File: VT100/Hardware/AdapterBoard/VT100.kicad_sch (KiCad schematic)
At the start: 40 parts, among them J1 GPIO, J2 RS232, J3 Vin < 12V DC / AC, J4 Mini-DIN-6, J5 zu Pi Zero, J6 USB_A, J7 Z80-MBC2 direct, J8 LCD Power, J9 On / Off, K1 G5V-2, Q2 BC546, Q3 BS170, U1 LM2576HVS-ADJ

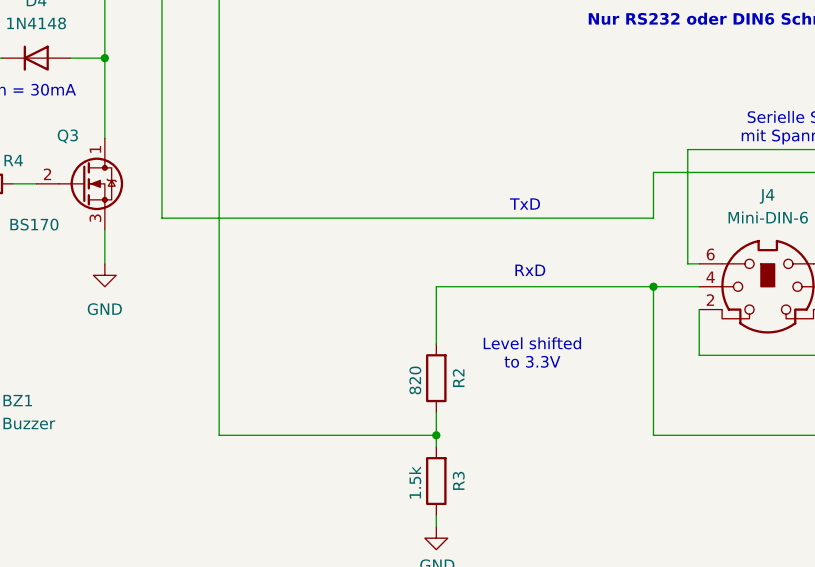
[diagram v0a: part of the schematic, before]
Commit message: VT100 AdapterBoard: add TxD level shifter
Add TxD level shifting network in AdapterBoard schematic and PCB routing.\n\nChanges include new resistor-based shift path and corresponding net/routing updates for TXD signal adaptation.
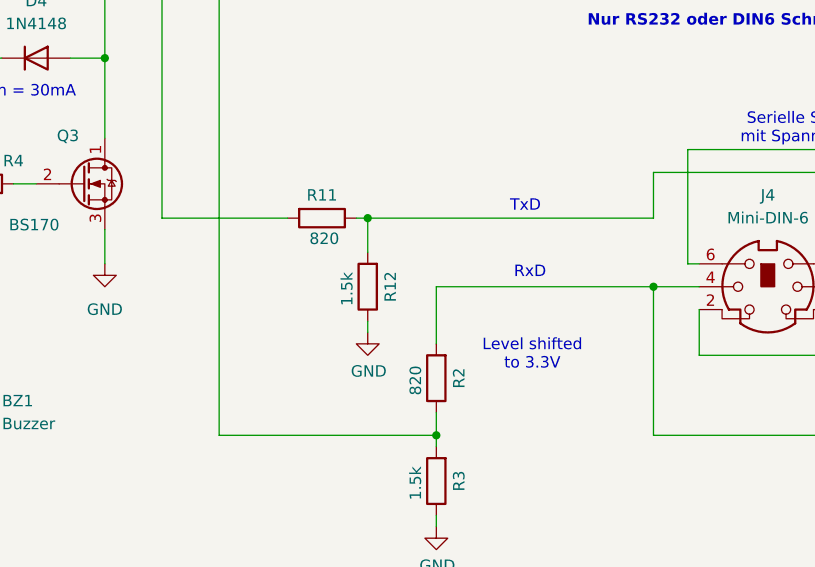
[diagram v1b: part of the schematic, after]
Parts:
- added R11: 820, Resistor_THT:R_Axial_DIN0207_L6.3mm_D2.5mm_P10.16mm_Horizontal, symbol Device:R
- added R12: 1.5k, Resistor_THT:R_Axial_DIN0207_L6.3mm_D2.5mm_P10.16mm_Horizontal, symbol Device:R
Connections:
- net GND: now also R12.1
- net at J2.2 (Pin_2), K1.6, K1.9: now also R11.2; no longer J4.3, J7.3 (Pin_3)
- new net: J4.3, J7.3 (Pin_3), R11.1, R12.2
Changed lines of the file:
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@@
 	)
 	(junction
+		(at 171.45 74.93)
+		(diameter 0)
+		(color 0 0 0 0)
+	)
+	(junction
 		(at 142.24 57.15)
 		(diameter 0)
@@
 	(wire
 		(pts
+			(xy 170.18 74.93) (xy 171.45 74.93)
+		)
+		(stroke
+			(width 0)
+			(type default)
+		)
+	)
+	(wire
+		(pts
 			(xy 73.66 35.56) (xy 82.55 35.56)
 		)
@@
 	(wire
 		(pts
+			(xy 171.45 74.93) (xy 171.45 78.74)
+		)
+		(stroke
+			(width 0)
+			(type default)
+		)
+	)
+	(wire
+		(pts
 			(xy 179.07 96.52) (xy 179.07 99.06)
 		)
@@
 	(wire
 		(pts
+			(xy 171.45 86.36) (xy 171.45 87.63)
+		)
+		(stroke
+			(width 0)
+			(type default)
+		)
+	)
+	(wire
+		(pts
 			(xy 58.42 38.1) (xy 60.96 38.1)
 		)
@@
 	(wire
 		(pts
+			(xy 171.45 74.93) (xy 203.2 74.93)
+		)
+		(stroke
+			(width 0)
+			(type default)
+		)
+	)
+	(wire
+		(pts
 			(xy 208.28 90.17) (xy 224.79 90.17)
 		)
@@
 	(wire
 		(pts
-			(xy 148.59 74.93) (xy 203.2 74.93)
+			(xy 148.59 74.93) (xy 162.56 74.93)
 		)
 		(stroke
@@
 	)
 	(symbol
+		(lib_id "Device:R")
+		(at 166.37 74.93 270)
+		(unit 1)
+		(exclude_from_sim no)
+		(in_bom yes)
+		(on_board yes)
+		(dnp no)
+		(property "Reference" "R11"
+			(at 166.37 72.39 90)
+			(effects
+				(font
+					(size 1.27 1.27)
+				)
+			)
+		)
+		(property "Value" "820"
+			(at 166.624 77.216 90)
+			(effects
+				(font
+					(size 1.27 1.27)
+				)
+			)
+		)
+		(property "Footprint" "Resistor_THT:R_Axial_DIN0207_L6.3mm_D2.5mm_P10.16mm_Horizontal"
+			(at 166.37 73.152 90)
+			(effects
+				(font
+					(size 1.27 1.27)
+				)
+				(hide yes)
+			)
+		)
+		(property "Datasheet" "~"
+			(at 166.37 74.93 0)
+			(effects
+				(font
+					(size 1.27 1.27)
+				)
+				(hide yes)
+			)
+		)
+		(property "Description" "Resistor"
+			(at 166.37 74.93 0)
+			(effects
+				(font
+					(size 1.27 1.27)
+				)
+				(hide yes)
+			)
+		)
+		(pin "2"
+		)
+		(pin "1"
+		)
+		(instances
+			(project "VT100"
+				(path "/e63e39d7-6ac0-4ffd-8aa3-1841a4541b55"
+					(reference "R11")
+					(unit 1)
+				)
+			)
+		)
+	)
+	(symbol
 		(lib_id "Mechanical:MountingHole")
 		(at 245.11 151.13 0)
@@
 	(symbol
 		(lib_id "Device:R")
+		(at 171.45 82.55 180)
+		(unit 1)
+		(exclude_from_sim no)
+		(in_bom yes)
+		(on_board yes)
+		(dnp no)
+		(property "Reference" "R12"
+			(at 173.99 82.55 90)
+			(effects
+				(font
+					(size 1.27 1.27)
+				)
+			)
+		)
+		(property "Value" "1.5k"
+			(at 169.164 82.804 90)
+			(effects
+				(font
+					(size 1.27 1.27)
+				)
+			)
+		)
+		(property "Footprint" "Resistor_THT:R_Axial_DIN0207_L6.3mm_D2.5mm_P10.16mm_Horizontal"
+			(at 173.228 82.55 90)
+			(effects
+				(font
+					(size 1.27 1.27)
+				)
+				(hide yes)
+			)
+		)
+		(property "Datasheet" "~"
+			(at 171.45 82.55 0)
+			(effects
+				(font
+					(size 1.27 1.27)
+				)
+				(hide yes)
+			)
+		)
+		(property "Description" "Resistor"
+			(at 171.45 82.55 0)
+			(effects
+				(font
+					(size 1.27 1.27)
+				)
+				(hide yes)
+			)
+		)
+		(pin "2"
+		)
+		(pin "1"
+		)
+		(instances
+			(project "VT100"
+				(path "/e63e39d7-6ac0-4ffd-8aa3-1841a4541b55"
+					(reference "R12")
+					(unit 1)
+				)
+			)
+		)
+	)
+	(symbol
+		(lib_id "Device:R")
 		(at 147.32 171.45 0)
 		(unit 1)
@@
 					(unit 1)
 				)
+			)
+		)
+	)
+	(symbol
+		(lib_id "power:GND")
+		(at 171.45 87.63 0)
+		(unit 1)
+		(exclude_from_sim no)
+		(in_bom yes)
+		(on_board yes)
+		(dnp no)
+		(property "Reference" "#PWR011"
+			(at 171.45 93.98 0)
+			(effects
+				(font
+					(size 1.27 1.27)
+				)
+				(hide yes)
+			)
+		)
+		(property "Value" "GND"
+			(at 171.5643 91.9544 0)
+			(effects
+				(font
+					(size 1.27 1.27)
+				)
+			)
+		)
+		(property "Footprint" ""
+			(at 171.45 87.63 0)
+			(effects
+				(font
+					(size 1.27 1.27)
+				)
+			)
+		)
+		(property "Datasheet" ""
+			(at 171.45 87.63 0)
+			(effects
+				(font
+					(size 1.27 1.27)
+				)
+			)
+		)
+		(property "Description" "Power symbol creates a global label with name \"GND\" , ground"
+			(at 171.45 87.63 0)
+			(effects
+				(font
+					(size 1.27 1.27)
+				)
+				(hide yes)
+			)
+		)
+		(pin "1"
+		)
+		(instances
+			(project "VT100"
+				(path "/e63e39d7-6ac0-4ffd-8aa3-1841a4541b55"
+					(reference "#PWR011")
+					(unit 1)
+				)
